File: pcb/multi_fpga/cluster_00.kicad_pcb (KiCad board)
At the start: 4 copper layers, 0 parts

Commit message: Fully routed. DRC-clean.
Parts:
- added A1: ~, Package_DIP:DIP-48_W15.24mm_Socket, F.Cu at (156.1, 94.3)
- added C1: 10uF, Capacitor_SMD:C_1206_3216Metric, F.Cu at (164.0, 153.0)
- added C18: 100nF, Capacitor_SMD:C_0603_1608Metric, F.Cu at (131.5, 37.0)
- added C19: 100nF, Capacitor_SMD:C_0603_1608Metric, F.Cu at (160.0, 63.0)
- added C2: 1uF, Capacitor_SMD:C_0603_1608Metric, F.Cu at (152.5, 54.5)
- added C20: 100nF, Capacitor_SMD:C_0603_1608Metric, F.Cu at (146.5, 49.0)
- added C21: 100nF, Capacitor_SMD:C_0603_1608Metric, F.Cu at (114.5, 28.0)
- added C22: 100nF, Capacitor_SMD:C_0603_1608Metric, F.Cu at (183.5, 93.5)
- added C23: 100nF, Capacitor_SMD:C_0603_1608Metric, F.Cu at (202.0, 127.0)
- added C24: 100nF, Capacitor_SMD:C_0603_1608Metric, F.Cu at (193.5, 110.0)
- added C25: 100nF, Capacitor_SMD:C_0603_1608Metric, F.Cu at (172.5, 78.0)
- added C26: 100nF, Capacitor_SMD:C_0603_1608Metric, F.Cu at (121.3, 56.5)
- added C27: 100nF, Capacitor_SMD:C_0603_1608Metric, F.Cu at (133.0, 93.5)
- added C28: 100nF, Capacitor_SMD:C_0603_1608Metric, F.Cu at (128.2, 74.5)
- added C29: 100nF, Capacitor_SMD:C_0603_1608Metric, F.Cu at (111.5, 40.5)
- added C3: 1uF, Capacitor_SMD:C_0603_1608Metric, F.Cu at (156.8, 60.5)
- added C30: 100nF, Capacitor_SMD:C_0603_1608Metric, F.Cu at (137.5, 131.5)
- added C31: 100nF, Capacitor_SMD:C_0603_1608Metric, F.Cu at (137.5, 170.0)
- added C32: 100nF, Capacitor_SMD:C_0603_1608Metric, F.Cu at (138.0, 151.0)
- added C33: 100nF, Capacitor_SMD:C_0603_1608Metric, F.Cu at (136.3, 112.5)
- added C34: 100nF, Capacitor_SMD:C_0603_1608Metric, F.Cu at (102.5, 68.5)
- added C35: 100nF, Capacitor_SMD:C_0603_1608Metric, F.Cu at (95.0, 106.0)
- added C36: 100nF, Capacitor_SMD:C_0603_1608Metric, F.Cu at (99.5, 87.5)
- added C37: 100nF, Capacitor_SMD:C_0603_1608Metric, F.Cu at (102.0, 49.5)
- added C38: 100nF, Capacitor_SMD:C_0603_1608Metric, F.Cu at (79.5, 141.5)
- added C39: 100nF, Capacitor_SMD:C_0603_1608Metric, F.Cu at (60.0, 175.0)
- added C40: 100nF, Capacitor_SMD:C_0603_1608Metric, F.Cu at (70.0, 158.5)
- added C41: 100nF, Capacitor_SMD:C_0603_1608Metric, F.Cu at (87.8, 124.0)
- added J1: Cluster0_SpokeBus, Connector_PinHeader_2.54mm:PinHeader_2x06_P2.54mm_Vertical, F.Cu at (133.6, 51.9)
- added J2: Cluster0_Power, Connector_PinHeader_2.54mm:PinHeader_1x02_P2.54mm_Vertical, F.Cu at (147.7, 57.0)
- added U1: IM72D128V01XTMA1, IM72D128:IFX-PG-LLGA-5-4, F.Cu at (115.1, 31.0)
- added U10: IM72D128V01XTMA1, IM72D128:IFX-PG-LLGA-5-4, F.Cu at (121.7, 60.0)
- added U11: IM72D128V01XTMA1, IM72D128:IFX-PG-LLGA-5-4, F.Cu at (128.6, 77.9)
- added U12: IM72D128V01XTMA1, IM72D128:IFX-PG-LLGA-5-4, F.Cu at (133.4, 96.6)
- added U13: IM72D128V01XTMA1, IM72D128:IFX-PG-LLGA-5-4, F.Cu at (136.4, 115.6)
- added U14: IM72D128V01XTMA1, IM72D128:IFX-PG-LLGA-5-4, F.Cu at (138.0, 134.8)
- added U15: IM72D128V01XTMA1, IM72D128:IFX-PG-LLGA-5-4, F.Cu at (138.4, 154.0)
- added U16: IM72D128V01XTMA1, IM72D128:IFX-PG-LLGA-5-4, F.Cu at (137.7, 173.3)
- added U17: IM72D128V01XTMA1, IM72D128:IFX-PG-LLGA-5-4, F.Cu at (102.6, 52.7)
- added U18: IM72D128V01XTMA1, IM72D128:IFX-PG-LLGA-5-4, F.Cu at (103.0, 71.9)
- added U19: IM72D128V01XTMA1, IM72D128:IFX-PG-LLGA-5-4, F.Cu at (100.0, 90.9)
- added U2: IM72D128V01XTMA1, IM72D128:IFX-PG-LLGA-5-4, F.Cu at (131.9, 40.3)
- added U20: IM72D128V01XTMA1, IM72D128:IFX-PG-LLGA-5-4, F.Cu at (94.8, 109.5)
- added U21: IM72D128V01XTMA1, IM72D128:IFX-PG-LLGA-5-4, F.Cu at (88.0, 127.4)
- added U22: IM72D128V01XTMA1, IM72D128:IFX-PG-LLGA-5-4, F.Cu at (79.7, 144.9)
- added U23: IM72D128V01XTMA1, IM72D128:IFX-PG-LLGA-5-4, F.Cu at (70.4, 161.7)
- added U24: IM72D128V01XTMA1, IM72D128:IFX-PG-LLGA-5-4, F.Cu at (60.2, 178.0)
- added U3: IM72D128V01XTMA1, IM72D128:IFX-PG-LLGA-5-4, F.Cu at (146.9, 52.3)
- added U4: IM72D128V01XTMA1, IM72D128:IFX-PG-LLGA-5-4, F.Cu at (160.4, 66.1)
- added U5: IM72D128V01XTMA1, IM72D128:IFX-PG-LLGA-5-4, F.Cu at (172.5, 81.1)
- added U6: IM72D128V01XTMA1, IM72D128:IFX-PG-LLGA-5-4, F.Cu at (183.5, 96.9)
- added U7: IM72D128V01XTMA1, IM72D128:IFX-PG-LLGA-5-4, F.Cu at (193.4, 113.4)
- added U8: IM72D128V01XTMA1, IM72D128:IFX-PG-LLGA-5-4, F.Cu at (202.4, 130.4)
- added U9: IM72D128V01XTMA1, IM72D128:IFX-PG-LLGA-5-4, F.Cu at (111.7, 43.5)
- added VR1: CP1700T-1802E/TT, Package_TO_SOT_SMD:SOT-23, F.Cu at (156.0, 57.0)
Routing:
- net C0_PDM_CLK: track 0.00 -> 501.9 mm
- net GND: track 0.00 -> 191.8 mm, vias 0 -> 51
- net SPOKE0_CLK: track 0.00 -> 143.0 mm
- net SPOKE0_STROBE: track 0.00 -> 141.6 mm, vias 0 -> 2
- net SPOKE0_D5: track 0.00 -> 134.8 mm
- net SPOKE0_D4: track 0.00 -> 134.1 mm, vias 0 -> 2
- net DATA_08: track 0.00 -> 125.9 mm, vias 0 -> 3
- net +5V: track 0.00 -> 119.7 mm, vias 0 -> 1
- net DATA_09: track 0.00 -> 118.7 mm, vias 0 -> 3
- net C0_1V8: track 0.00 -> 114.2 mm, vias 0 -> 25
- net SPOKE0_D2: track 0.00 -> 110.9 mm, vias 0 -> 2
- net SPOKE0_D0: track 0.00 -> 108.0 mm
- net DATA_10: track 0.00 -> 106.7 mm, vias 0 -> 3
- net SPOKE0_D3: track 0.00 -> 106.5 mm
- net SPOKE0_D1: track 0.00 -> 103.7 mm
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- added copper zone on In2.Cu, net C0_1V8
- added copper zone on In1.Cu, net GND
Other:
- board outline added: 208.8 x 161.7 mm

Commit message: Added reset and alive signals.
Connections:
- A1 pad 30: unconnected-(A1-PIO30-Pad30) -> FPGA_RESET_N
- A1 pad 31: unconnected-(A1-PIO31-Pad31) -> SPOKE0_ALIVE
- J1 pad 11: GND -> FPGA_RESET_N
- J1 pad 12: GND -> SPOKE0_ALIVE
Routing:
- net FPGA_RESET_N: track 0.00 -> 100.4 mm, vias 0 -> 1
- net SPOKE0_ALIVE: track 0.00 -> 96.1 mm, vias 0 -> 1
- net DATA_07: track 103.1 -> 105.7 mm
- net SPOKE0_D2: track 110.9 -> 112.6 mm
- net SPOKE0_D4: track 134.1 -> 135.5 mm
- net DATA_05: track 62.0 -> 60.9 mm
- net SPOKE0_STROBE: track 141.6 -> 142.3 mm
- net DATA_04: track 82.9 -> 83.5 mm

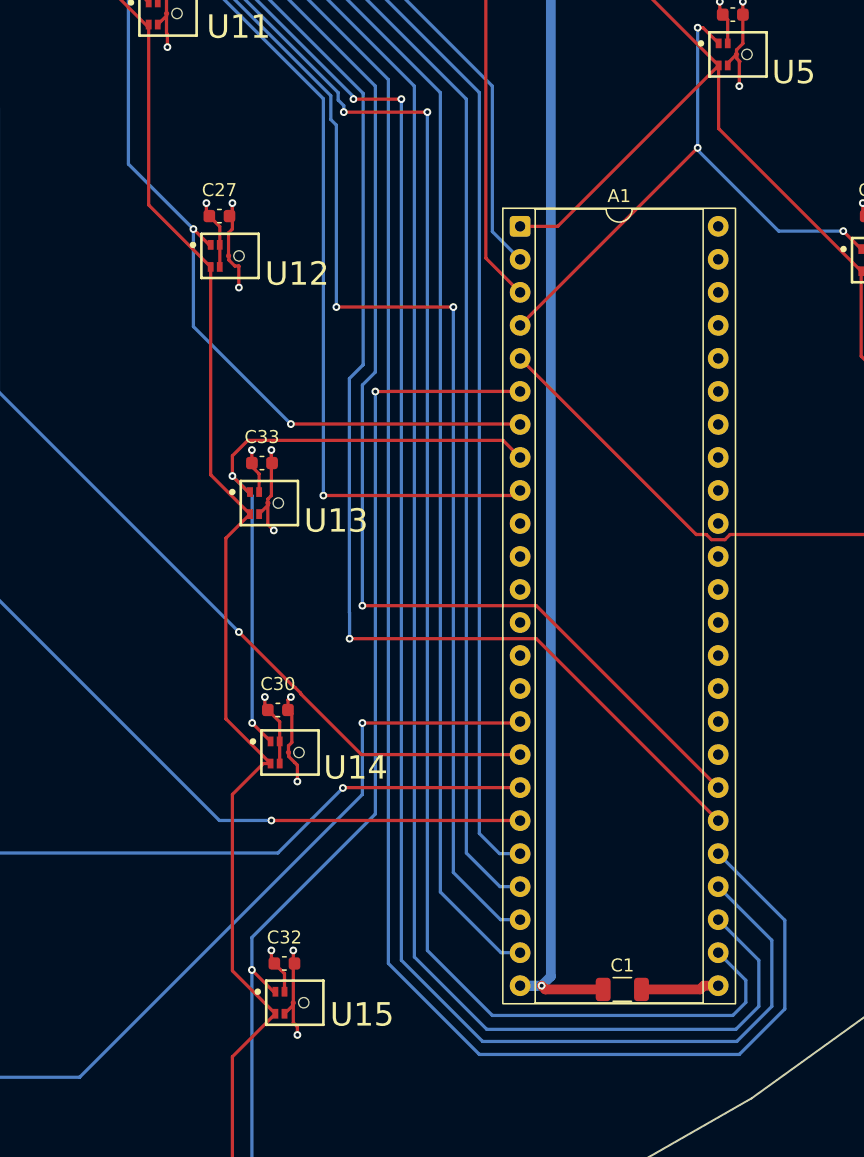
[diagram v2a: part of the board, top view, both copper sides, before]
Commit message: Moved clock pin.
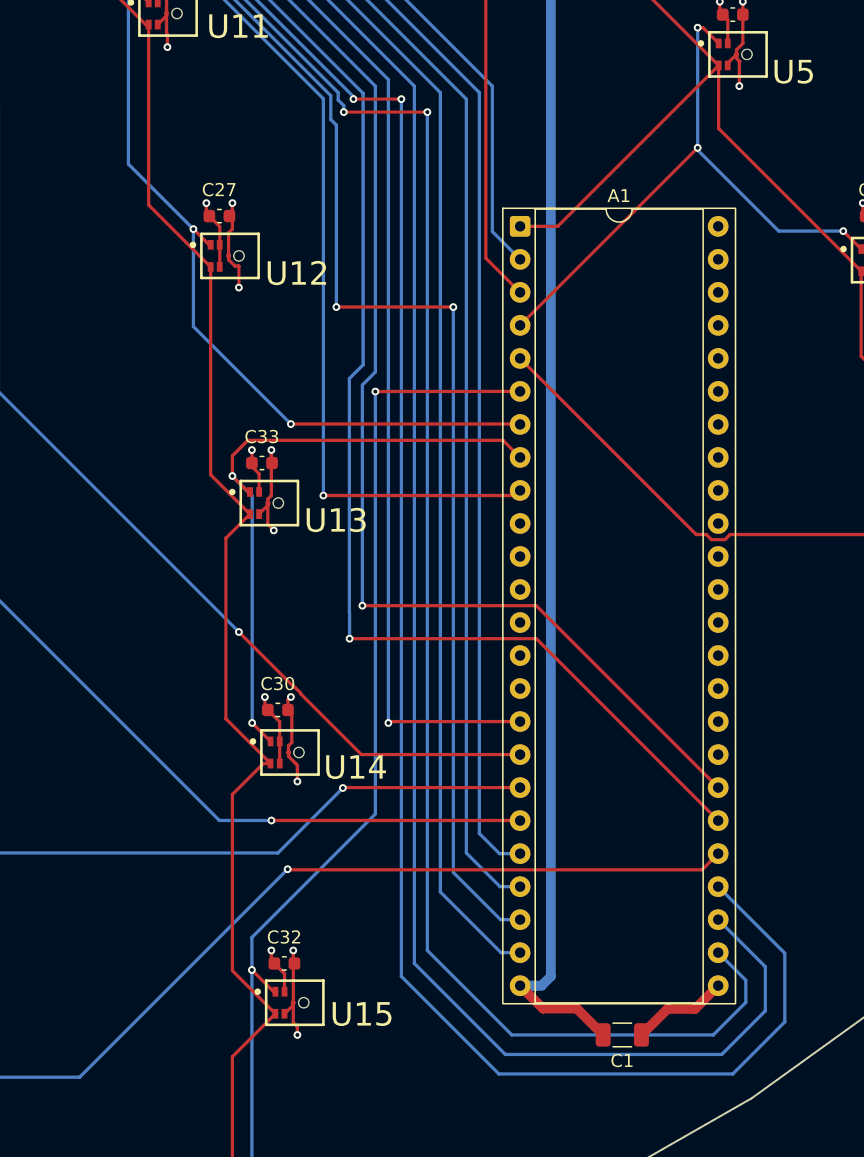
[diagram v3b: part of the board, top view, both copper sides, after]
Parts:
- moved C1 3.50 mm to (164.0, 156.5)
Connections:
- A1 pad 16: DATA_08 -> SPOKE0_CLK
- A1 pad 29: SPOKE0_CLK -> DATA_08
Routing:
- net SPOKE0_CLK: track 143.0 -> 86.0 mm, vias 0 -> 1
- net DATA_08: track 125.9 -> 134.0 mm
- net SPOKE0_STROBE: track 142.3 -> 147.2 mm
- net +5V: track 119.7 -> 122.9 mm, vias 1 -> 0
- net SPOKE0_D5: track 134.8 -> 137.6 mm
- net GND: track 191.8 -> 193.2 mm
- net SPOKE0_D4: track 135.5 -> 136.8 mm

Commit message: Switched to use only cluster_00 pcb.
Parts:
- added H1A: MountingHole_2.7mm_M2.5, MountingHole:MountingHole_2.7mm_M2.5, F.Cu at (145.4, 73.4)
- added H1E1: MountingHole_3.2mm_M3, MountingHole:MountingHole_3.2mm_M3, F.Cu at (211.5, 100.8)
- added H1E2: MountingHole_3.2mm_M3, MountingHole:MountingHole_3.2mm_M3, F.Cu at (42.5, 162.7)
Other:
- board text added: "${UNIT_ID}"

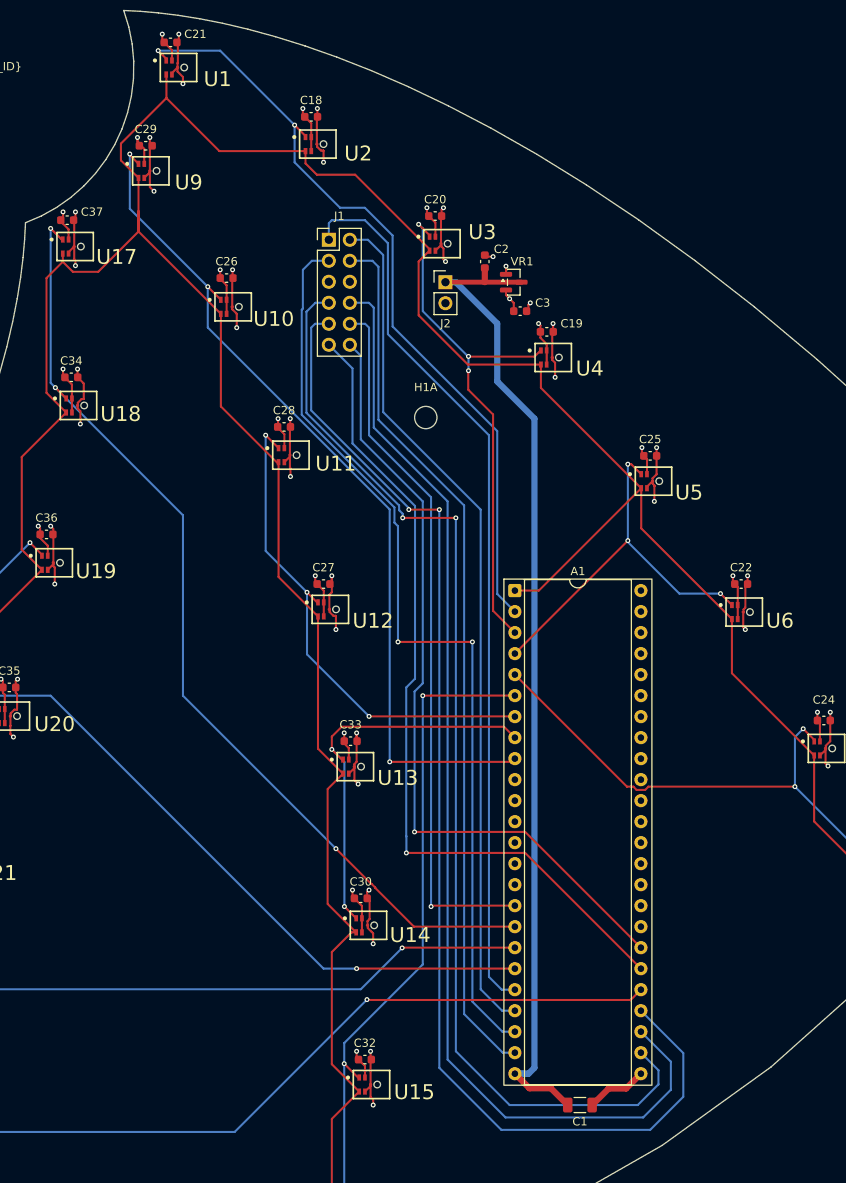
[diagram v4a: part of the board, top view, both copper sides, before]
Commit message: Swapped to proper clock pin.
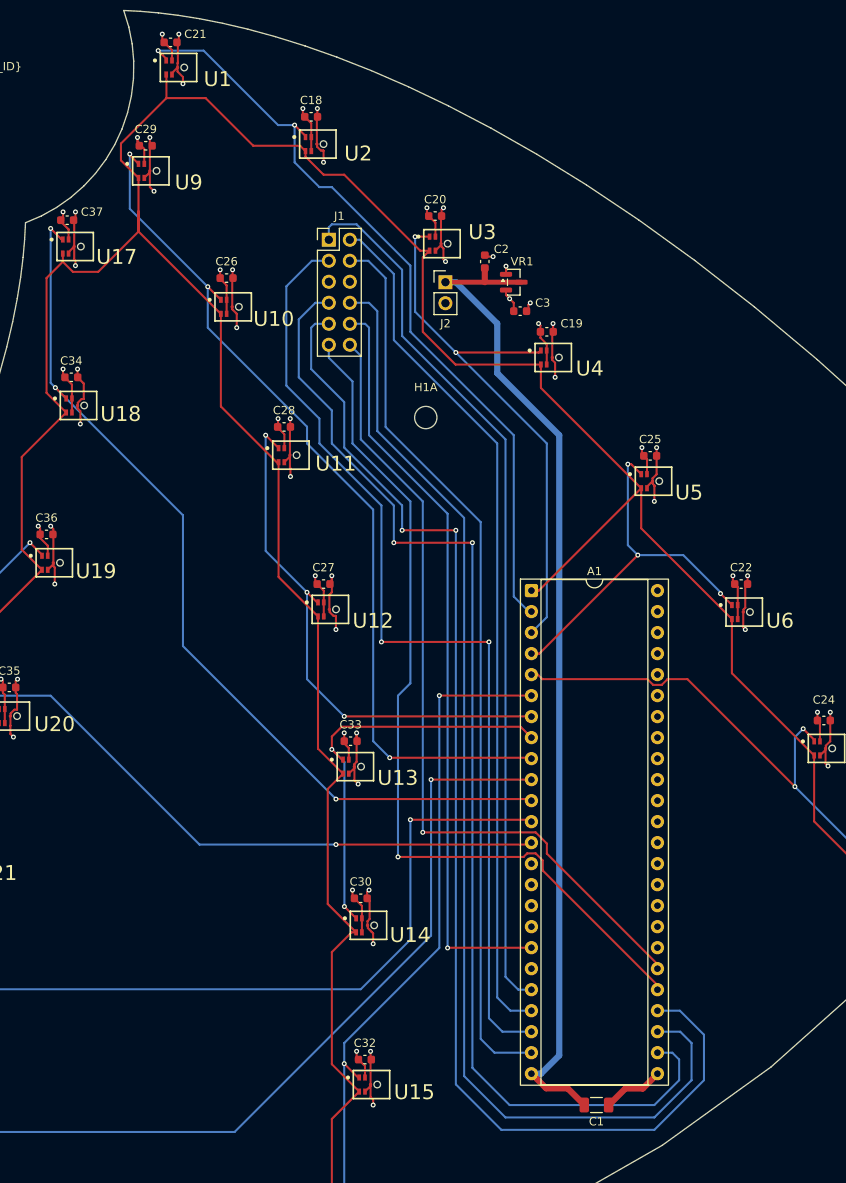
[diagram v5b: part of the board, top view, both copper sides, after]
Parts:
- moved A1 2.00 mm to (158.1, 94.3)
- moved C1 2.00 mm to (166.0, 156.5)
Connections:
- A1 pad 10: (no net) -> DATA_08
- A1 pad 11: (no net) -> DATA_09
- A1 pad 12: (no net) -> DATA_10
- A1 pad 13: (no net) -> DATA_11
- A1 pad 14: (no net) -> unconnected-(A1-PIO14-Pad14)
- A1 pad 15: (no net) -> unconnected-(A1-AIN15-Pad15)
- A1 pad 16: SPOKE0_CLK -> unconnected-(A1-AIN16-Pad16)
- A1 pad 17: DATA_09 -> unconnected-(A1-PIO17-Pad17)
- A1 pad 18: DATA_10 -> SPOKE0_CLK
- A1 pad 19: DATA_11 -> unconnected-(A1-PIO19-Pad19)
- A1 pad 29: DATA_08 -> FPGA_RESET_N
- A1 pad 30: FPGA_RESET_N -> SPOKE0_ALIVE
- A1 pad 31: SPOKE0_ALIVE -> unconnected-(A1-PIO31-Pad31)
- A1 pad 34: (no net) -> unconnected-(A1-PIO34-Pad34)
- A1 pad 35: (no net) -> unconnected-(A1-PIO35-Pad35)
- A1 pad 36: (no net) -> unconnected-(A1-PIO36-Pad36)
- A1 pad 37: (no net) -> unconnected-(A1-PIO37-Pad37)
- A1 pad 38: (no net) -> unconnected-(A1-PIO38-Pad38)
- A1 pad 39: (no net) -> unconnected-(A1-PIO39-Pad39)
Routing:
- net DATA_10: track 106.7 -> 123.7 mm
- net DATA_08: track 134.0 -> 142.3 mm
- net DATA_09: track 118.7 -> 110.9 mm
- net SPOKE0_D4: track 136.8 -> 142.8 mm
- net SPOKE0_D2: track 112.6 -> 118.5 mm
- net FPGA_RESET_N: track 100.4 -> 106.1 mm
- net SPOKE0_CLK: track 86.0 -> 91.6 mm
- net SPOKE0_STROBE: track 147.2 -> 152.0 mm
- net DATA_11: track 102.2 -> 98.1 mm
- net DATA_05: track 60.9 -> 64.6 mm
- net SPOKE0_D5: track 137.6 -> 141.2 mm
- net SPOKE0_ALIVE: track 96.1 -> 98.8 mm
- net SPOKE0_D3: track 106.5 -> 108.8 mm
- net DATA_01: track 65.4 -> 67.5 mm, vias 3 -> 2
- net C0_PDM_CLK: track 501.9 -> 499.8 mm
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
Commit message: Changed to 3V3.
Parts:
- VR1: value CP1700T-1802E/TT -> MCP1700x-330xxTT
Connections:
- net C0_1V8 renamed C0_3V3
